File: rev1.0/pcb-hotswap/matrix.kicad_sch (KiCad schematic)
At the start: 94 parts

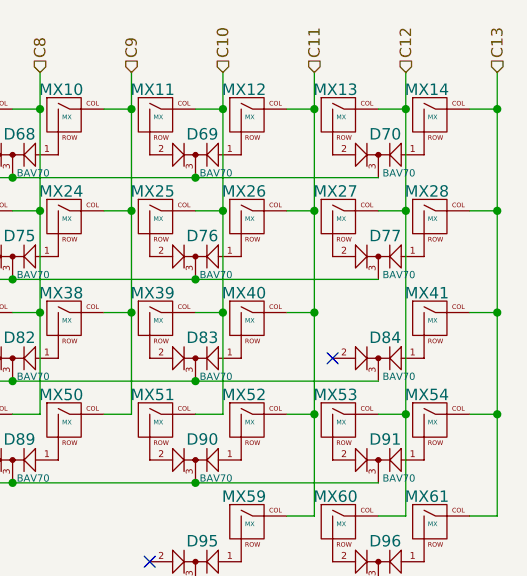
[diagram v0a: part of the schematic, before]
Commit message: Change "\" matrix position on hotswap PCB to match soldered PCB
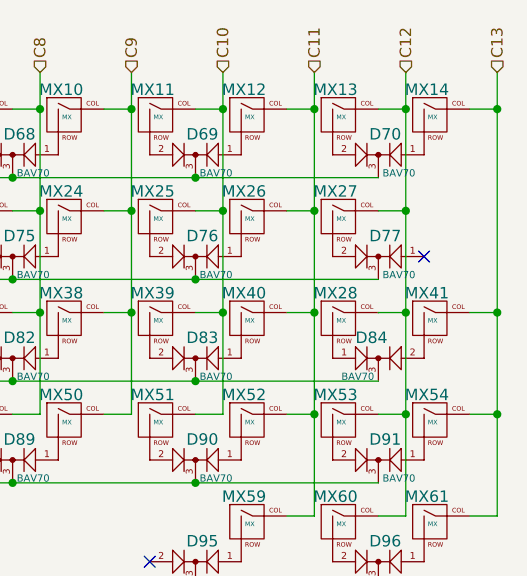
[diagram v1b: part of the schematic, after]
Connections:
- net C12: now also MX28.1 (COL)
- net C13: no longer MX28.1 (COL)
- net at D84.1 (A1): now also MX28.2 (ROW); no longer MX41.2 (ROW)
- net at D84.2 (A2): now also MX41.2 (ROW)
- net at D77.1 (A1): no longer MX28.2 (ROW)
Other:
- moved on the sheet: MX28
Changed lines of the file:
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@@
   (junction (at 122.428 43.561) (diameter 0) (color 0 0 0 0)
   )
-  (junction (at 176.276 47.244) (diameter 0) (color 0 0 0 0)
-  )
   (junction (at 74.676 47.244) (diameter 0) (color 0 0 0 0)
   )
@@
   )
   (junction (at 145.796 47.244) (diameter 0) (color 0 0 0 0)
+  )
+  (junction (at 166.116 58.5493) (diameter 0) (color 0 0 0 0)
   )
   (junction (at 135.636 35.941) (diameter 0) (color 0 0 0 0)
@@
   (no_connect (at 66.548 86.233))
   (no_connect (at 137.668 86.233))
-  (no_connect (at 157.988 63.627))
+  (no_connect (at 168.148 52.324))
   (wire (pts (xy 115.316 58.547) (xy 115.316 47.244))
     (stroke (width 0) (type solid) (color 0 0 0 0))
@@
     (stroke (width 0) (type solid) (color 0 0 0 0))
   )
+  (wire (pts (xy 166.116 58.5493) (xy 163.068 58.5493))
+    (stroke (width 0) (type default) (color 0 0 0 0))
+  )
   (wire (pts (xy 94.996 47.244) (xy 94.996 35.941))
     (stroke (width 0) (type solid) (color 0 0 0 0))
@@
     (stroke (width 0) (type solid) (color 0 0 0 0))
   )
-  (wire (pts (xy 166.116 47.244) (xy 166.116 69.85))
+  (wire (pts (xy 166.116 47.244) (xy 166.116 58.5493))
     (stroke (width 0) (type solid) (color 0 0 0 0))
   )
@@
     (stroke (width 0) (type solid) (color 0 0 0 0))
   )
+  (wire (pts (xy 163.068 58.5493) (xy 163.068 58.547))
+    (stroke (width 0) (type default) (color 0 0 0 0))
+  )
   (wire (pts (xy 155.956 81.153) (xy 155.956 69.85))
     (stroke (width 0) (type solid) (color 0 0 0 0))
@@
     (stroke (width 0) (type solid) (color 0 0 0 0))
   )
-  (wire (pts (xy 176.276 58.547) (xy 176.276 47.244))
+  (wire (pts (xy 176.276 35.941) (xy 176.276 58.547))
     (stroke (width 0) (type solid) (color 0 0 0 0))
   )
@@
     (stroke (width 0) (type solid) (color 0 0 0 0))
   )
-  (wire (pts (xy 173.228 47.244) (xy 176.276 47.244))
-    (stroke (width 0) (type solid) (color 0 0 0 0))
-  )
   (wire (pts (xy 166.116 35.941) (xy 163.068 35.941))
     (stroke (width 0) (type solid) (color 0 0 0 0))
@@
     (stroke (width 0) (type solid) (color 0 0 0 0))
   )
+  (wire (pts (xy 166.116 58.5493) (xy 166.116 69.85))
+    (stroke (width 0) (type solid) (color 0 0 0 0))
+  )
   (wire (pts (xy 54.356 81.153) (xy 51.308 81.153))
     (stroke (width 0) (type solid) (color 0 0 0 0))
@@
   )
   (wire (pts (xy 32.893 88.773) (xy 41.148 88.773))
-    (stroke (width 0) (type solid) (color 0 0 0 0))
-  )
-  (wire (pts (xy 176.276 47.244) (xy 176.276 35.941))
     (stroke (width 0) (type solid) (color 0 0 0 0))
   )
@@
     (pin "2")
   )
-  (symbol (lib_id "0xCB:BAV70") (at 163.068 63.627 0) (mirror y) (unit 1)
-    (in_bom yes) (on_board yes)
-    (property "Reference" "D84" (id 0) (at 163.83 61.341 0))
-    (property "Value" "BAV70" (id 1) (at 165.354 65.659 0)
-      (effects (font (size 0.8 0.8)))
-    )
-    (property "Footprint" "Package_TO_SOT_SMD:SOT-23" (id 2) (at 161.798 72.009 0)
-      (effects (font (size 1.27 1.27)) hide)
-    )
-    (property "Datasheet" "https://assets.nexperia.com/documents/data-sheet/BAV70_SER.pdf" (id 3) (at 160.782 73.533 0)
+  (symbol (lib_id "0xCB:BAV70") (at 163.068 63.627 0) (unit 1)
+    (in_bom yes) (on_board yes)
+    (property "Reference" "D84" (id 0) (at 162.306 61.341 0))
+    (property "Value" "BAV70" (id 1) (at 160.782 65.659 0)
+      (effects (font (size 0.8 0.8)))
+    )
+    (property "Footprint" "Package_TO_SOT_SMD:SOT-23" (id 2) (at 164.338 72.009 0)
+      (effects (font (size 1.27 1.27)) hide)
+    )
+    (property "Datasheet" "https://assets.nexperia.com/documents/data-sheet/BAV70_SER.pdf" (id 3) (at 165.354 73.533 0)
       (effects (font (size 1.27 1.27)) hide)
     )
@@
     (pin "2")
   )
-  (symbol (lib_id "0xCB:MX") (at 169.418 47.244 0) (unit 1)
-    (in_bom yes) (on_board yes)
-    (property "Reference" "MX28" (id 0) (at 168.4655 45.085 0))
-    (property "Value" "MX" (id 1) (at 169.1005 48.133 0)
-      (effects (font (size 0.508 0.508)))
-    )
-    (property "Footprint" "0xCB:SW_Hotswap_Kailh_1.50u" (id 2) (at 170.688 44.704 0)
-      (effects (font (size 1.27 1.27)) hide)
-    )
-    (property "Datasheet" "" (id 3) (at 170.688 44.704 0)
-      (effects (font (size 1.27 1.27)) hide)
-    )
+  (symbol (lib_id "0xCB:MX") (at 159.258 58.547 0) (unit 1)
+    (in_bom yes) (on_board yes)
+    (property "Reference" "MX28" (id 0) (at 158.3055 56.388 0))
+    (property "Value" "MX" (id 1) (at 158.9405 59.436 0)
+      (effects (font (size 0.508 0.508)))
+    )
+    (property "Footprint" "0xCB:SW_Hotswap_Kailh_1.50u" (id 2) (at 160.528 56.007 0)
+      (effects (font (size 1.27 1.27)) hide)
+    )
+    (property "Datasheet" "" (id 3) (at 160.528 56.007 0)
+      (effects (font (size 1.27 1.27)) hide)
+    )
